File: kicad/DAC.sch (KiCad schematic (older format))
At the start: 27 parts, among them Q1 Q_DUAL_NMOS_S1G1D2S2G2D1, U6 VRH4801NTX, U7 DS3911, U8 TSV994IPT

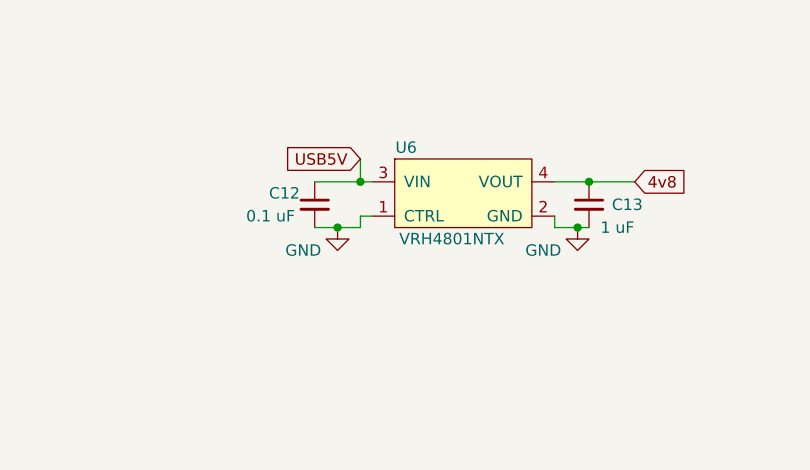
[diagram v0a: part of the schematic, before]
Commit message: replaced 4v8 reg
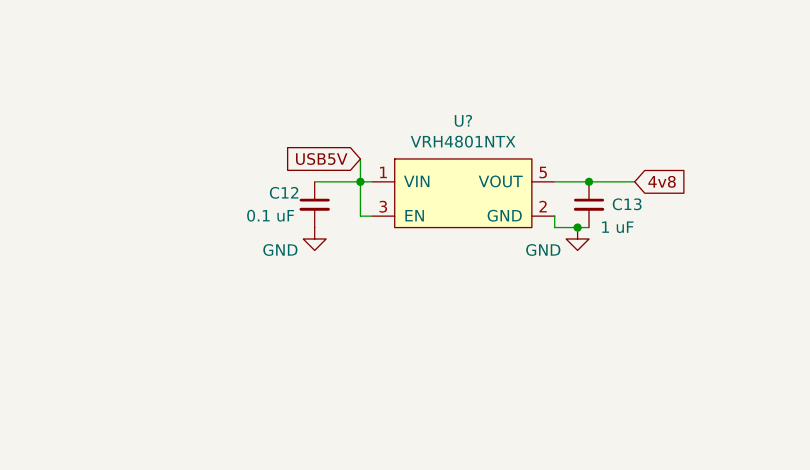
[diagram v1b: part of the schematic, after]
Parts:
- removed U6: VRH4801NTX, Package_TO_SOT_SMD:SOT-553, symbol quadrant:TCR2EE
- added U?: VRH4801NTX, quadrant:SOT-25, symbol quadrant:VRH4801NTX
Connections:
- net 4v8: now also U?.5 (VOUT)
- net GND: now also U?.2 (GND)
- net USB5V: now also U?.1 (VIN), U?.3 (EN)
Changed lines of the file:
@@
 Wire Wire Line
 	8800 4600 9150 4600
-$Comp
-L quadrant:TCR2EE U?
-U 1 1 63AF8548
-P 4550 3550
-AR Path="/63AF8548" Ref="U?"  Part="1"
-AR Path="/63922B28/63AF8548" Ref="U6"  Part="1"
-F 0 "U6" H 4300 3750 50  0000 C CNN
-F 1 "VRH4801NTX" H 4500 3350 50  0000 C CNN
-F 2 "Package_TO_SOT_SMD:SOT-553" H 4550 3550 50  0001 C CNN
-F 3 "" H 4550 3550 50  0001 C CNN
-F 4 "https://www.digikey.com/en/products/detail/toshiba-semiconductor-and-storage/TCR2EE48-LM/5114341" H 4550 3550 50  0001 C CNN "digikey"
-F 5 "SOT-23-5" H 4550 3550 50  0001 C CNN "JLC"
-F 6 "C698019" H 4550 3550 50  0001 C CNN "LCSC"
-F 7 "---" H 4550 3550 50  0001 C CNN "ordered"
-	1    4550 3550
-	1    0    0    -1
-$EndComp
 Wire Wire Line
 	4150 3500 4100 3500
@@
 Wire Wire Line
 	3900 3500 4100 3500
-Wire Wire Line
-	3900 3700 4000 3700
-Wire Wire Line
-	4100 3700 4100 3650
 $Comp
 L power:GND #PWR?
@@
 L power:GND #PWR?
 U 1 1 63AF856E
-P 4000 3700
+P 3900 3700
 AR Path="/63AF856E" Ref="#PWR?"  Part="1"
 AR Path="/63922B28/63AF856E" Ref="#PWR040"  Part="1"
-F 0 "#PWR040" H 4000 3450 50  0001 C CNN
-F 1 "GND" H 3850 3600 50  0000 C CNN
-F 2 "" H 4000 3700 50  0001 C CNN
-F 3 "" H 4000 3700 50  0001 C CNN
-	1    4000 3700
-	1    0    0    -1
-$EndComp
-Connection ~ 4000 3700
-Wire Wire Line
-	4000 3700 4100 3700
+F 0 "#PWR040" H 3900 3450 50  0001 C CNN
+F 1 "GND" H 3750 3600 50  0000 C CNN
+F 2 "" H 3900 3700 50  0001 C CNN
+F 3 "" H 3900 3700 50  0001 C CNN
+	1    3900 3700
+	1    0    0    -1
+$EndComp
 Text GLabel 5300 3500 2    50   Input ~ 0
 4v8
@@
 Wire Wire Line
 	8800 4100 9150 4100
+$Comp
+L quadrant:VRH4801NTX U?
+U 1 1 6386062D
+P 4550 3550
+F 0 "U?" H 4550 3865 50  0000 C CNN
+F 1 "VRH4801NTX" H 4550 3774 50  0000 C CNN
+F 2 "quadrant:SOT-25" H 4550 3550 50  0001 C CNN
+F 3 "" H 4550 3550 50  0001 C CNN
+	1    4550 3550
+	1    0    0    -1
+$EndComp
+Wire Wire Line
+	4100 3650 4100 3500
 $EndSCHEMATC
